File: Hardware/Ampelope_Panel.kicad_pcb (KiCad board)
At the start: 2 copper layers, 60.8 x 128.5 mm, 28 parts

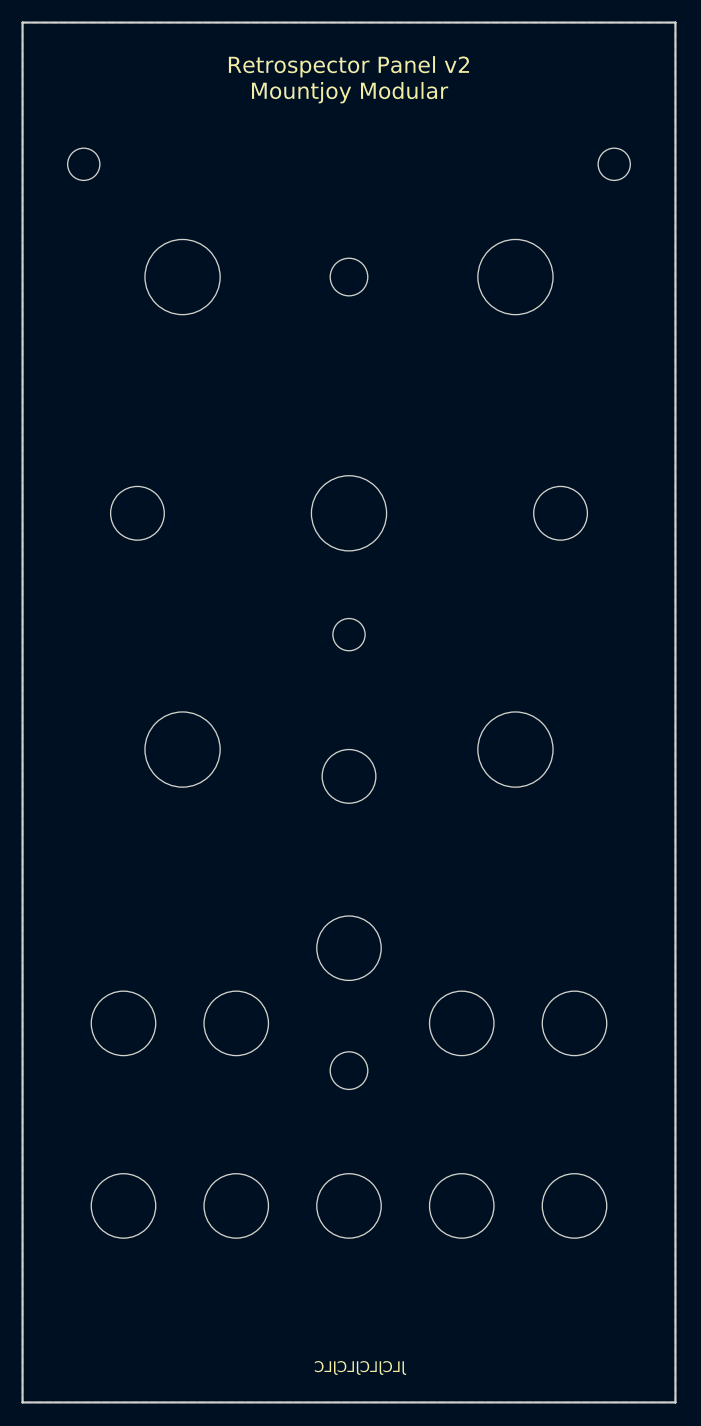
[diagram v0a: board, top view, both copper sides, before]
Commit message: Draft of panel layout
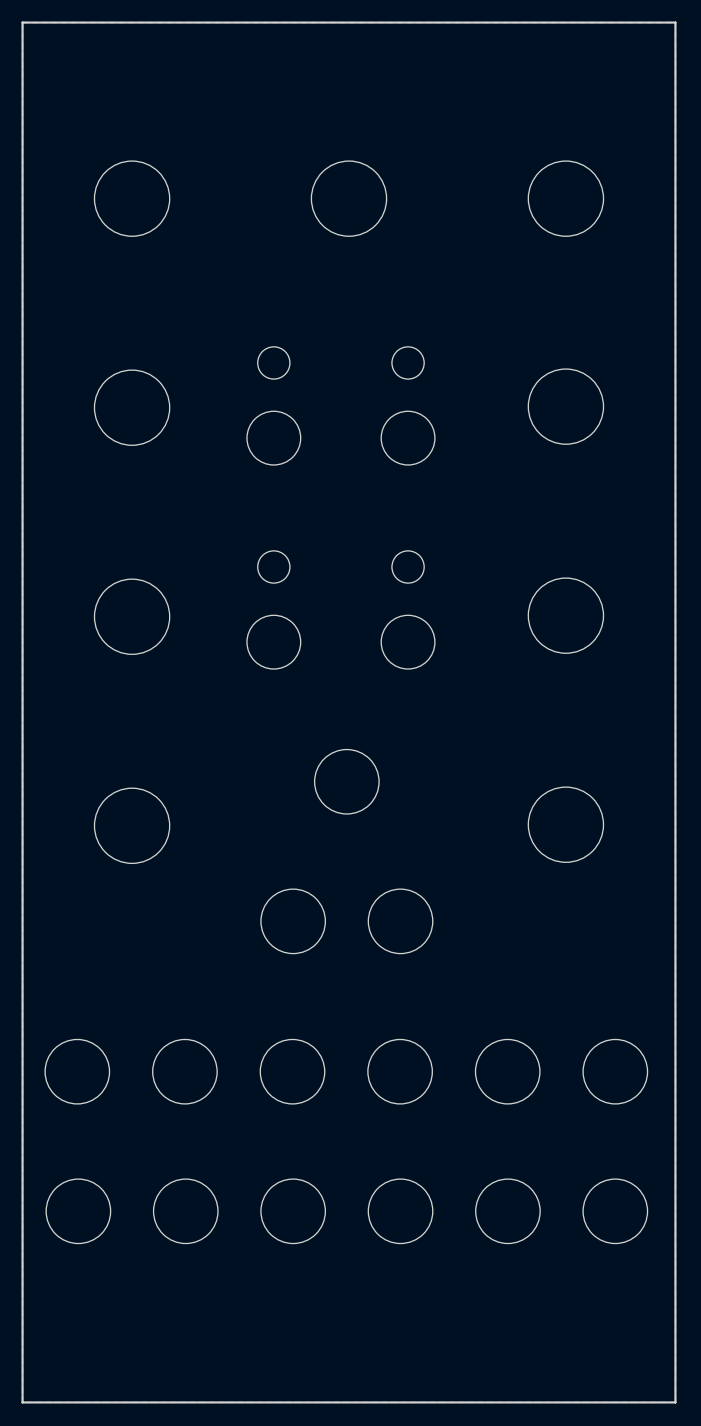
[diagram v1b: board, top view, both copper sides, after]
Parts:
- removed DELAY_L, DELAY_R, FEEDBACK, TONE: Alpha_9mm_pot_hole, Custom_Footprints:Alpha_9mm_pot_hole
- removed the LED_L at (154.7, 54.0)
- removed LED_R (x2): Subminiature_Switch, Custom_Footprints:LED_Hole_3mm
- removed MODE: Subminiature_Switch, Custom_Footprints:Sub_Miniature_Switch_MountingHole_5mm
- removed RESET (x2): Subminiature_Switch, Custom_Footprints:Small_Pushbutton_Hole_3.5mm
- removed the Ref** at (140.5, 134.0)
- removed the Ref** at (151.0, 151.0)
- removed the Ref** at (151.0, 134.0)
- removed the Ref** at (140.5, 151.0)
- removed the Ref** at (130.0, 151.0)
- removed the Ref** at (109.0, 134.0)
- removed the Ref** at (119.5, 134.0)
- removed the Ref** at (119.5, 151.0)
- removed the Ref** at (130.0, 127.0)
- removed the TYPE at (130.0, 111.0)
- removed the TYPE at (110.3, 86.5)
- added LED_L: Subminiature_Switch, Custom_Footprints:LED_Hole_3mm, F.Cu at (123.0, 72.5)
- added LED_L: LED_Hole_3mm, Custom_Footprints:LED_Hole_3mm, F.Cu at (135.5, 91.5)
- added LED_L: LED_Hole_3mm, Custom_Footprints:LED_Hole_3mm, F.Cu at (123.0, 91.5)
- added MIX: Alpha_9mm_pot_hole, Custom_Footprints:Alpha_9mm_pot_hole, F.Cu at (150.2, 96.0)
- added MIX: Alpha_9mm_pot_hole, Custom_Footprints:Alpha_9mm_pot_hole, F.Cu at (130.0, 57.2)
- added MIX: Alpha_9mm_pot_hole, Custom_Footprints:Alpha_9mm_pot_hole, F.Cu at (150.2, 76.6)
- added MIX: Alpha_9mm_pot_hole, Custom_Footprints:Alpha_9mm_pot_hole, F.Cu at (109.8, 96.1)
- added MIX: Alpha_9mm_pot_hole, Custom_Footprints:Alpha_9mm_pot_hole, F.Cu at (109.8, 57.2)
- added MIX: Alpha_9mm_pot_hole, Custom_Footprints:Alpha_9mm_pot_hole, F.Cu at (109.8, 76.7)
- added MIX: Alpha_9mm_pot_hole, Custom_Footprints:Alpha_9mm_pot_hole, F.Cu at (150.2, 57.2)
- added MIX: Alpha_9mm_pot_hole, Custom_Footprints:Alpha_9mm_pot_hole, F.Cu at (109.8, 115.6)
- added Ref**: Thonkiconn_Socket_MountingHole_6mm, Custom_Footprints:Thonkiconn_Socket_MountingHole_6mm, F.Cu at (124.8, 124.5)
- added Ref**: Thonkiconn_Socket_MountingHole_6mm, Custom_Footprints:Thonkiconn_Socket_MountingHole_6mm, F.Cu at (134.8, 138.5)
- added Ref**: LED_Hole_3mm, Custom_Footprints:LED_Hole_3mm, F.Cu at (135.5, 72.5)
- added Ref**: Thonkiconn_Socket_MountingHole_6mm, Custom_Footprints:Thonkiconn_Socket_MountingHole_6mm, F.Cu at (144.8, 151.5)
- added Ref**: Thonkiconn_Socket_MountingHole_6mm, Custom_Footprints:Thonkiconn_Socket_MountingHole_6mm, F.Cu at (104.7, 138.5)
- added Ref**: Thonkiconn_Socket_MountingHole_6mm, Custom_Footprints:Thonkiconn_Socket_MountingHole_6mm, F.Cu at (124.8, 151.5)
- added Ref**: Thonkiconn_Socket_MountingHole_6mm, Custom_Footprints:Thonkiconn_Socket_MountingHole_6mm, F.Cu at (129.8, 111.5)
- added Ref**: Thonkiconn_Socket_MountingHole_6mm, Custom_Footprints:Thonkiconn_Socket_MountingHole_6mm, F.Cu at (104.8, 151.5)
- added Ref**: Thonkiconn_Socket_MountingHole_6mm, Custom_Footprints:Thonkiconn_Socket_MountingHole_6mm, F.Cu at (134.8, 124.5)
- added Ref**: Thonkiconn_Socket_MountingHole_6mm, Custom_Footprints:Thonkiconn_Socket_MountingHole_6mm, F.Cu at (124.7, 138.5)
- added Ref**: Thonkiconn_Socket_MountingHole_6mm, Custom_Footprints:Thonkiconn_Socket_MountingHole_6mm, F.Cu at (144.8, 138.5)
- added Ref**: Thonkiconn_Socket_MountingHole_6mm, Custom_Footprints:Thonkiconn_Socket_MountingHole_6mm, F.Cu at (134.8, 151.5)
- added Ref**: Thonkiconn_Socket_MountingHole_6mm, Custom_Footprints:Thonkiconn_Socket_MountingHole_6mm, F.Cu at (114.7, 138.5)
- added Ref**: Thonkiconn_Socket_MountingHole_6mm, Custom_Footprints:Thonkiconn_Socket_MountingHole_6mm, F.Cu at (154.8, 138.5)
- added Ref**: Thonkiconn_Socket_MountingHole_6mm, Custom_Footprints:Thonkiconn_Socket_MountingHole_6mm, F.Cu at (114.8, 151.5)
- added TYPE: Subminiature_Switch, Custom_Footprints:Sub_Miniature_Switch_MountingHole_5mm, F.Cu at (123.0, 98.5)
- added TYPE: Subminiature_Switch, Custom_Footprints:Sub_Miniature_Switch_MountingHole_5mm, F.Cu at (135.5, 79.5)
- added TYPE: Subminiature_Switch, Custom_Footprints:Sub_Miniature_Switch_MountingHole_5mm, F.Cu at (135.5, 98.5)
- added TYPE: Subminiature_Switch, Custom_Footprints:Sub_Miniature_Switch_MountingHole_5mm, F.Cu at (123.0, 79.5)
- G***, MIX, Ref**: moved to F.Cu
- moved Ref** 45.8 mm to (154.8, 151.5), turned to 180 degrees
- moved MIX 36.4 mm to (150.2, 115.5), turned to 180 degrees
- turned G*** to 0 degrees
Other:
- board text added: "Ampelope Panel v1 Mountjoy Modular"
- board text removed: "Retrospector Panel v2 Mountjoy Modular"

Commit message: Work on panel and control layout
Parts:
- removed the G*** at (129.5, 44.9)
- added G***: LOGO, Logo_Footprint:logo, F.Cu at (130.3, 45.2)
- moved Ref** 4.30 mm to (139.1, 124.6)
- moved Ref** 3.30 mm to (121.5, 124.6)
- moved Ref** 2.35 mm to (130.3, 113.8)
- moved Ref** 2.16 mm to (136.7, 70.7)
- moved TYPE 2.16 mm to (136.7, 77.7)
- moved LED_L 2.01 mm to (123.9, 70.7)
- moved TYPE 2.01 mm to (123.9, 77.7)
- moved LED_L 1.24 mm to (136.7, 91.2)
- moved TYPE 1.24 mm to (136.7, 98.2)
- moved Ref** 1.17 mm to (125.2, 152.6)
- moved Ref** 1.17 mm to (105.2, 152.6)
- moved Ref** 1.17 mm to (115.2, 152.6)
- moved Ref** 1.17 mm to (145.2, 152.6)
- moved Ref** 1.17 mm to (155.2, 152.6)
- moved Ref** 1.17 mm to (135.2, 152.6)
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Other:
- board text added: "1"
- board text added: "2"
- board text added: "3"
- board text added: "4"
- board text added: "A"
- board text added: "D"
- board text added: "Env Out"
- board text added: "Gate"
- board text added: "LFO"
- board text added: "S"
- board text added: "T"
- board text removed: "Chorus"
- board text removed: "Del L"
- board text removed: "Del R"
- board text removed: "Delay L"
- board text removed: "Delay R"
- board text removed: "Dry/Wet"
- board text removed: "Feedback"
- board text removed: "Filter"
- board text removed: "HP"
- board text removed: "LP"
- board text removed: "Link"
- board text removed: "Reset"
- board text removed: "Reverse"
- board text removed: "Short"
- board text removed: "Wide"

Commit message: First draft of panel and control boards complete
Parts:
- moved LED_L 16.0 mm to (141.7, 106.4)
- moved LED_L 16.0 mm to (118.9, 106.4)
- moved LED_L 5.64 mm to (118.9, 68.1)
- moved Ref** 5.64 mm to (141.7, 68.1)
- moved MIX 4.10 mm to (130.3, 61.4)
- moved TYPE 3.00 mm to (123.9, 95.2)
- moved TYPE 3.00 mm to (136.7, 95.2)
- moved Ref** 2.39 mm to (120.2, 126.6)
- moved Ref** 2.33 mm to (140.3, 126.6)
- moved Ref** 1.70 mm to (130.3, 115.5)
- moved TYPE 1.60 mm to (136.7, 79.3)
- moved TYPE 1.60 mm to (123.9, 79.3)
- moved G*** 0.60 mm to (130.3, 44.6)
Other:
- board text added: "Env"
- board text added: "Tremolo"
- board text removed: "Env Out"
- board text removed: "L"
- board text removed: "LFO"
- board text removed: "T"

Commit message: Various schematic and PCB tidying
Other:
- board text added: "Ampelope Panel v1.0 Mountjoy Modular 2021"
- board text removed: "Ampelope Panel v1 Mountjoy Modular"

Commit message: Further PCB tidy up and DAC testing
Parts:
- added REF**: Placeholder_Controls, Fiducial:Fiducial_0.5mm_Mask1.5mm, B.Cu at (99.9, 50.0)
- added REF**: Placeholder_Components, Fiducial:Fiducial_0.5mm_Mask1.5mm, B.Cu at (160.7, 50.0)
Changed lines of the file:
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@@
+    )
+  )
+  (footprint "Fiducial:Fiducial_0.5mm_Mask1.5mm" (layer "B.Cu")
+    (at 99.9 50 180)
+    (descr "Circular Fiducial, 0.5mm bare copper, 1.5mm soldermask opening")
+    (tags "fiducial")
+    (attr smd)
+    (fp_text reference "REF**" (at 0 1.7145) (layer "B.SilkS") hide
+      (effects (font (size 1 1) (thickness 0.15)) (justify mirror))
+    )
+    (fp_text value "Placeholder_Controls" (at 0 -1.7145) (layer "B.Fab")
+      (effects (font (size 1 1) (thickness 0.15)) (justify mirror))
+    )
+    (fp_text user "${REFERENCE}" (at 0 0) (layer "B.Fab")
+      (effects (font (size 0.2 0.2) (thickness 0.04)) (justify mirror))
+    )
+    (fp_circle (center 0 0) (end 1 0) (layer "B.CrtYd") (width 0.05) (fill none))
+    (model "${KIPRJMOD}/3d_models/Ampelope_Controls.step"
+      (offset (xyz -0.3 0 12))
+      (scale (xyz 1 1 1))
+      (rotate (xyz 0 180 0))
+    )
+  )
+  (footprint "Fiducial:Fiducial_0.5mm_Mask1.5mm" (layer "B.Cu")
+    (at 160.7 50 180)
+    (descr "Circular Fiducial, 0.5mm bare copper, 1.5mm soldermask opening")
+    (tags "fiducial")
+    (attr smd)
+    (fp_text reference "REF**" (at 0 1.7145) (layer "B.SilkS") hide
+      (effects (font (size 1 1) (thickness 0.15)) (justify mirror))
+    )
+    (fp_text value "Placeholder_Components" (at 0 -1.7145) (layer "B.Fab")
+      (effects (font (size 1 1) (thickness 0.15)) (justify mirror))
+    )
+    (fp_text user "${REFERENCE}" (at 0 0) (layer "B.Fab")
+      (effects (font (size 0.2 0.2) (thickness 0.04)) (justify mirror))
+    )
+    (fp_circle (center 0 0) (end 1 0) (layer "B.CrtYd") (width 0.05) (fill none))
+    (model "${KIPRJMOD}/3d_models/Ampelope_Components.step"
+      (offset (xyz 0 0 22))
+      (scale (xyz 1 1 1))
+      (rotate (xyz 0 0 0))
     )
   )
   (gr_line (start 138.3 70.9) (end 141.7 68.1) (layer "F.Mask") (width 0.2))
-  (gr_line (start 150.5 96.1) (end 156.4 90.2) (layer "F.Mask") (width 0.2))
+  (gr_line (start 150.5 96.1) (end 155.7 89.7) (layer "F.Mask") (width 0.2))
   (gr_line (start 130.3 82.401777) (end 130.3 82.198222) (layer "F.Mask") (width 0.6))
   (gr_line (start 120.2 126.55) (end 120.2 138.65) (layer "F.Mask") (width 0.2))
@@
       (xy 109.7 134.2)
     ) (layer "F.Mask") (width 0.8) (fill solid))
-  (gr_line (start 150.5 76.7) (end 156.4 70.8) (layer "F.Mask") (width 0.2))
+  (gr_line (start 150.5 76.7) (end 155.7 70.3) (layer "F.Mask") (width 0.2))
   (gr_poly
     (pts
@@
   (gr_line (start 124 79.1) (end 124 74.1) (layer "F.Mask") (width 0.2))
   (gr_circle (center 105.179063 130.2) (end 107.1 130.2) (layer "F.Mask") (width 0.2) (fill none))
-  (gr_line (start 110.1 57.3) (end 104.2 51.4) (layer "F.Mask") (width 0.2))
+  (gr_line (start 110.1 57.3) (end 104.9 50.9) (layer "F.Mask") (width 0.2))
   (gr_poly
     (pts
@@
     ) (layer "F.Mask") (width 0.8) (fill solid))
   (gr_line (start 131.8375 95.45) (end 128.7625 95.45) (layer "F.Mask") (width 0.6))
-  (gr_circle (center 157.8 69.3) (end 159.8 69.3) (layer "F.Mask") (width 0.2) (fill none))
-  (gr_line (start 110.1 115.5) (end 104.2 109.6) (layer "F.Mask") (width 0.2))
+  (gr_circle (center 157 68.7) (end 159 68.7) (layer "F.Mask") (width 0.2) (fill none))
+  (gr_line (start 110.1 115.5) (end 104.9 109.1) (layer "F.Mask") (width 0.2))
   (gr_line (start 130.465602 82.403555) (end 130.134398 82.4) (layer "F.Mask") (width 0.6))
-  (gr_circle (center 102.8 69.3) (end 104.8 69.3) (layer "F.Mask") (width 0.2) (fill none))
-  (gr_circle (center 157.8 88.7) (end 159.8 88.7) (layer "F.Mask") (width 0.2) (fill none))
+  (gr_circle (center 103.6 68.7) (end 105.6 68.7) (layer "F.Mask") (width 0.2) (fill none))
+  (gr_circle (center 157 88.1) (end 159 88.1) (layer "F.Mask") (width 0.2) (fill none))
   (gr_poly
     (pts
@@
       (xy 124.4 122.4)
     ) (layer "F.Mask") (width 0.8) (fill solid))
-  (gr_line (start 150.5 115.5) (end 156.4 109.6) (layer "F.Mask") (width 0.2))
+  (gr_line (start 150.5 115.5) (end 155.7 109.1) (layer "F.Mask") (width 0.2))
   (gr_line (start 155.2 138.7) (end 135.3 138.7) (layer "F.Mask") (width 0.8))
   (gr_line (start 155.2 153.379063) (end 155.2 158.579063) (layer "F.Mask") (width 0.2))
@@
   (gr_line (start 131.1 92.5) (end 129.5 92.5) (layer "F.Mask") (width 0.6))
   (gr_line (start 105.2 132.1) (end 105.2 137.3) (layer "F.Mask") (width 0.2))
-  (gr_circle (center 102.8 108.1) (end 104.8 108.1) (layer "F.Mask") (width 0.2) (fill none))
-  (gr_circle (center 157.8 108.1) (end 159.8 108.1) (layer "F.Mask") (width 0.2) (fill none))
+  (gr_circle (center 103.6 107.5) (end 105.6 107.5) (layer "F.Mask") (width 0.2) (fill none))
+  (gr_circle (center 157 107.5) (end 159 107.5) (layer "F.Mask") (width 0.2) (fill none))
   (gr_line (start 129.065602 98.401777) (end 129.065602 98.198222) (layer "F.Mask") (width 0.6))
   (gr_line (start 129.1 82.401777) (end 129.1 82.198222) (layer "F.Mask") (width 0.6))
@@
   (gr_line (start 138.3 103.6) (end 141.7 106.4) (layer "F.Mask") (width 0.2))
   (gr_circle (center 155.2 160.5) (end 157.120937 160.5) (layer "F.Mask") (width 0.2) (fill none))
-  (gr_circle (center 102.8 88.7) (end 104.8 88.7) (layer "F.Mask") (width 0.2) (fill none))
+  (gr_circle (center 103.6 88.1) (end 105.6 88.1) (layer "F.Mask") (width 0.2) (fill none))
   (gr_line (start 130.3 98.401777) (end 130.3 98.198222) (layer "F.Mask") (width 0.6))
   (gr_line (start 130.3 133.8) (end 130.3 133.8) (layer "F.Mask") (width 0.1))
@@
   (gr_line (start 118.9 68.1) (end 122.4 70.9) (layer "F.Mask") (width 0.2))
   (gr_line (start 123.9 95.2) (end 123.9 100.4) (layer "F.Mask") (width 0.2))
-  (gr_circle (center 157.8 49.9) (end 157.8 47.9) (layer "F.Mask") (width 0.2) (fill none))
+  (gr_circle (center 157 49.3) (end 157 47.3) (layer "F.Mask") (width 0.2) (fill none))
   (gr_line (start 131.665602 82.403555) (end 131.334398 82.4) (layer "F.Mask") (width 0.6))
   (gr_line (start 125.2 152.6) (end 105.25 152.6) (layer "F.Mask") (width 0.8))
   (gr_line (start 131.8375 79.45) (end 128.7625 79.45) (layer "F.Mask") (width 0.6))
-  (gr_line (start 110.1 96.1) (end 104.2 90.2) (layer "F.Mask") (width 0.2))
+  (gr_line (start 110.1 96.1) (end 104.9 89.7) (layer "F.Mask") (width 0.2))
   (gr_line (start 155.2 132.320937) (end 155.2 137.520937) (layer "F.Mask") (width 0.2))
   (gr_line (start 118.9 106.4) (end 122.3 103.6) (layer "F.Mask") (width 0.2))
-  (gr_line (start 110.1 76.7) (end 104.2 70.8) (layer "F.Mask") (width 0.2))
-  (gr_line (start 150.5 57.3) (end 156.4 51.4) (layer "F.Mask") (width 0.2))
+  (gr_line (start 110.1 76.7) (end 104.9 70.3) (layer "F.Mask") (width 0.2))
+  (gr_line (start 150.5 57.3) (end 155.7 50.9) (layer "F.Mask") (width 0.2))
   (gr_line (start 130.3 78.75) (end 128.7625 79.45) (layer "F.Mask") (width 0.6))
   (gr_line (start 131.5 82.401777) (end 131.5 82.198222) (layer "F.Mask") (width 0.6))
@@
   (gr_line (start 129.231204 98.403555) (end 128.9 98.4) (layer "F.Mask") (width 0.6))
   (gr_line (start 105.179063 153.279063) (end 105.179063 158.479063) (layer "F.Mask") (width 0.2))
-  (gr_circle (center 102.8 49.9) (end 104.8 49.9) (layer "F.Mask") (width 0.2) (fill none))
+  (gr_circle (center 103.6 49.3) (end 105.6 49.3) (layer "F.Mask") (width 0.2) (fill none))
   (gr_line (start 129.265602 82.403555) (end 128.934398 82.4) (layer "F.Mask") (width 0.6))
   (gr_line (start 136.7 95.2) (end 136.7 100.4) (layer "F.Mask") (width 0.2))
@@
     (effects (font (size 1 1) (thickness 0.15)) (justify mirror))
   )
-  (gr_text "A" (at 102.8 49.9) (layer "F.Mask")
-    (effects (font (size 2 2) (thickness 0.3)))
-  )
-  (gr_text "D" (at 102.8 69.3) (layer "F.Mask")
+  (gr_text "A" (at 103.6 49.3) (layer "F.Mask")
+    (effects (font (size 2 2) (thickness 0.3)))
+  )
+  (gr_text "D" (at 103.6 68.7) (layer "F.Mask")
     (effects (font (size 2 2) (thickness 0.3)))
   )
@@
     (effects (font (size 2 2) (thickness 0.3)))
   )
-  (gr_text "S" (at 157.8 88.7) (layer "F.Mask")
-    (effects (font (size 2 2) (thickness 0.3)))
-  )
-  (gr_text "R" (at 102.8 108.1) (layer "F.Mask")
-    (effects (font (size 2 2) (thickness 0.3)))
-  )
-  (gr_text "R" (at 157.8 108.1) (layer "F.Mask")
+  (gr_text "S" (at 157 88.1) (layer "F.Mask")
+    (effects (font (size 2 2) (thickness 0.3)))
+  )
+  (gr_text "R" (at 103.6 107.5) (layer "F.Mask")
+    (effects (font (size 2 2) (thickness 0.3)))
+  )
+  (gr_text "R" (at 157 107.5) (layer "F.Mask")
     (effects (font (size 2 2) (thickness 0.3)))
   )
@@
     (effects (font (size 2 2) (thickness 0.3)))
   )
-  (gr_text "D" (at 157.8 69.3) (layer "F.Mask")
+  (gr_text "D" (at 157 68.7) (layer "F.Mask")
     (effects (font (size 2 2) (thickness 0.3)))
   )
@@
     (effects (font (size 2 2) (thickness 0.3)))
   )
-  (gr_text "A" (at 157.9 49.9) (layer "F.Mask")
+  (gr_text "A" (at 157 49.3) (layer "F.Mask")
     (effects (font (size 2 2) (thickness 0.3)))
   )
@@
     (effects (font (size 2 2) (thickness 0.3)))
   )
-  (gr_text "S" (at 102.8 88.7) (layer "F.Mask")
-    (effects (font (size 2 2) (thickness 0.3)))
-  )
+  (gr_text "S" (at 103.6 88.1) (layer "F.Mask")
+    (effects (font (size 2 2) (thickness 0.3)))
+  )
